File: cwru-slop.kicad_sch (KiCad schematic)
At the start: 44 parts, among them J1 USB_C_Receptacle_USB2.0_16P, J2 FTSH-105-01-L-DV-007-K, SW1 SW_SPDT, U1 TLV9001IDCK, U10 B3U-1000P, U2 AP63205WU, U3 TLV75533PDBV, U4 STM32L433CCTx, U5 TPS2116DRL, U6 FXLS8974CFR3, U7 ESDCAN24-2BLY, U8 MCP2562-E-SN, U9 24lc32at-i/ot, Y1 XRCGB24M000F3M00R0

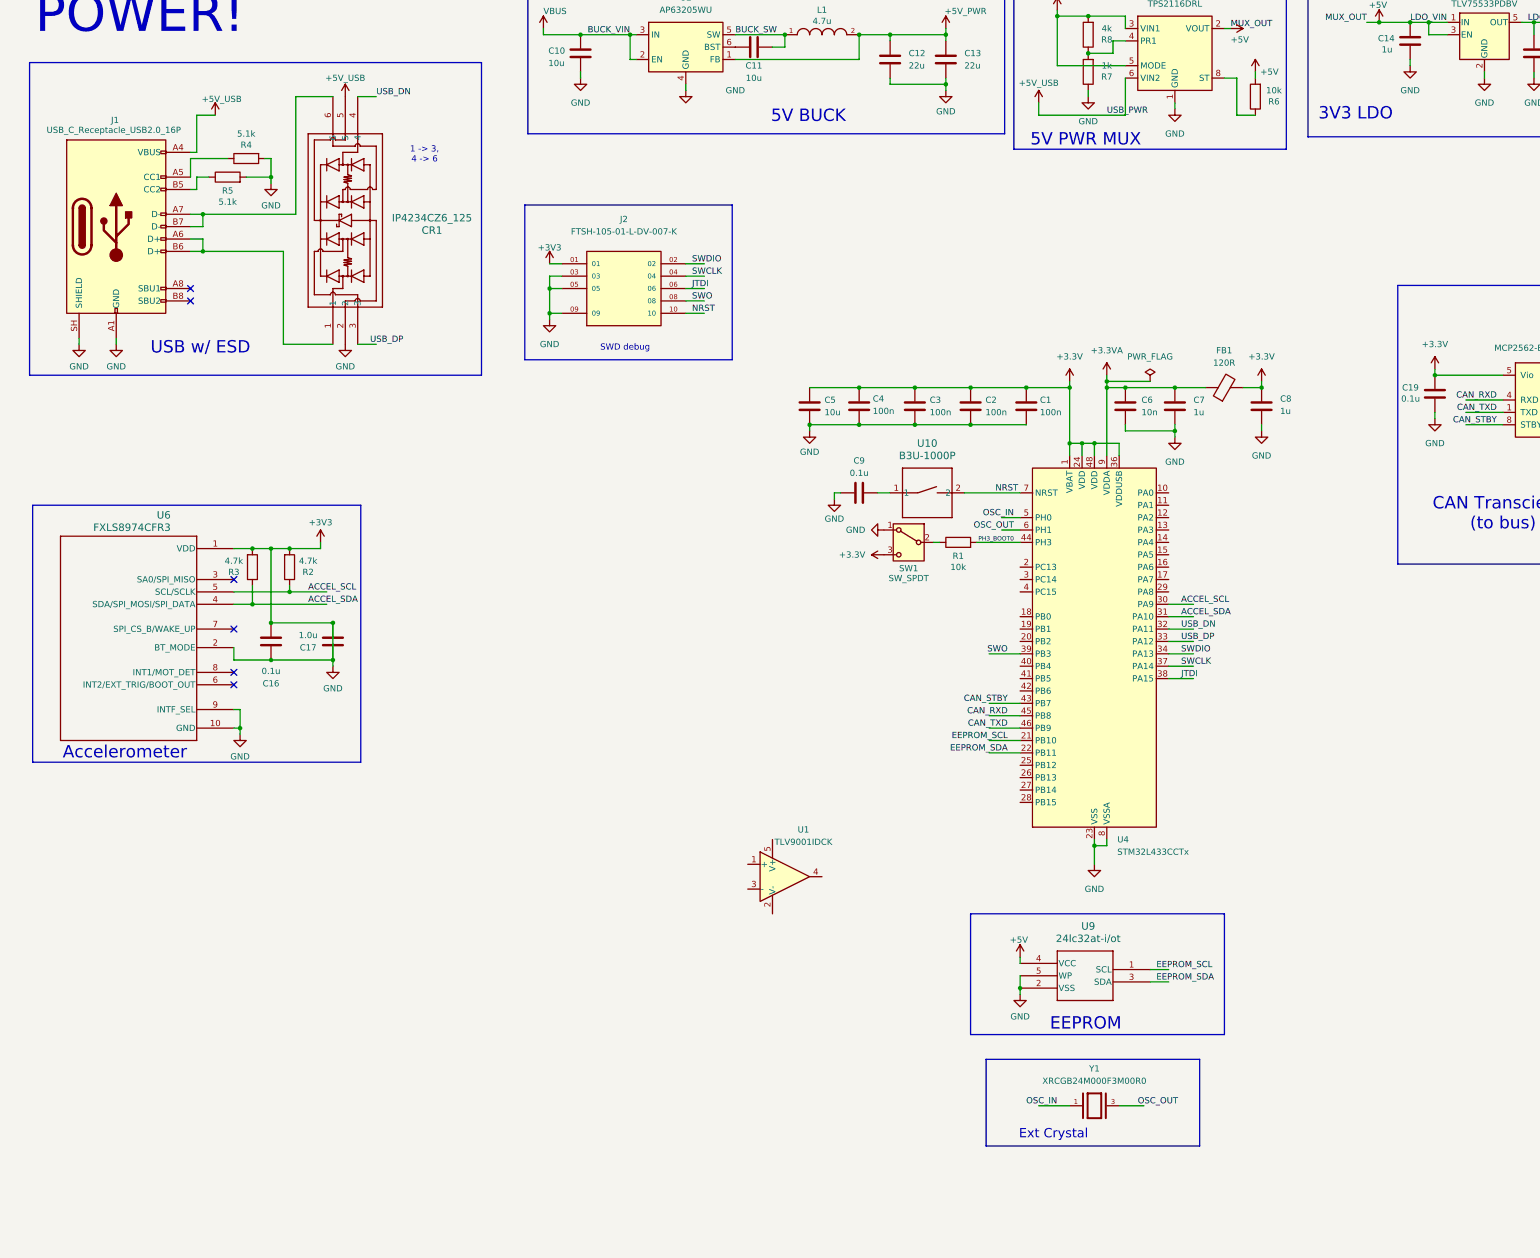
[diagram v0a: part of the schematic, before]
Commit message: analog inputs and filtering
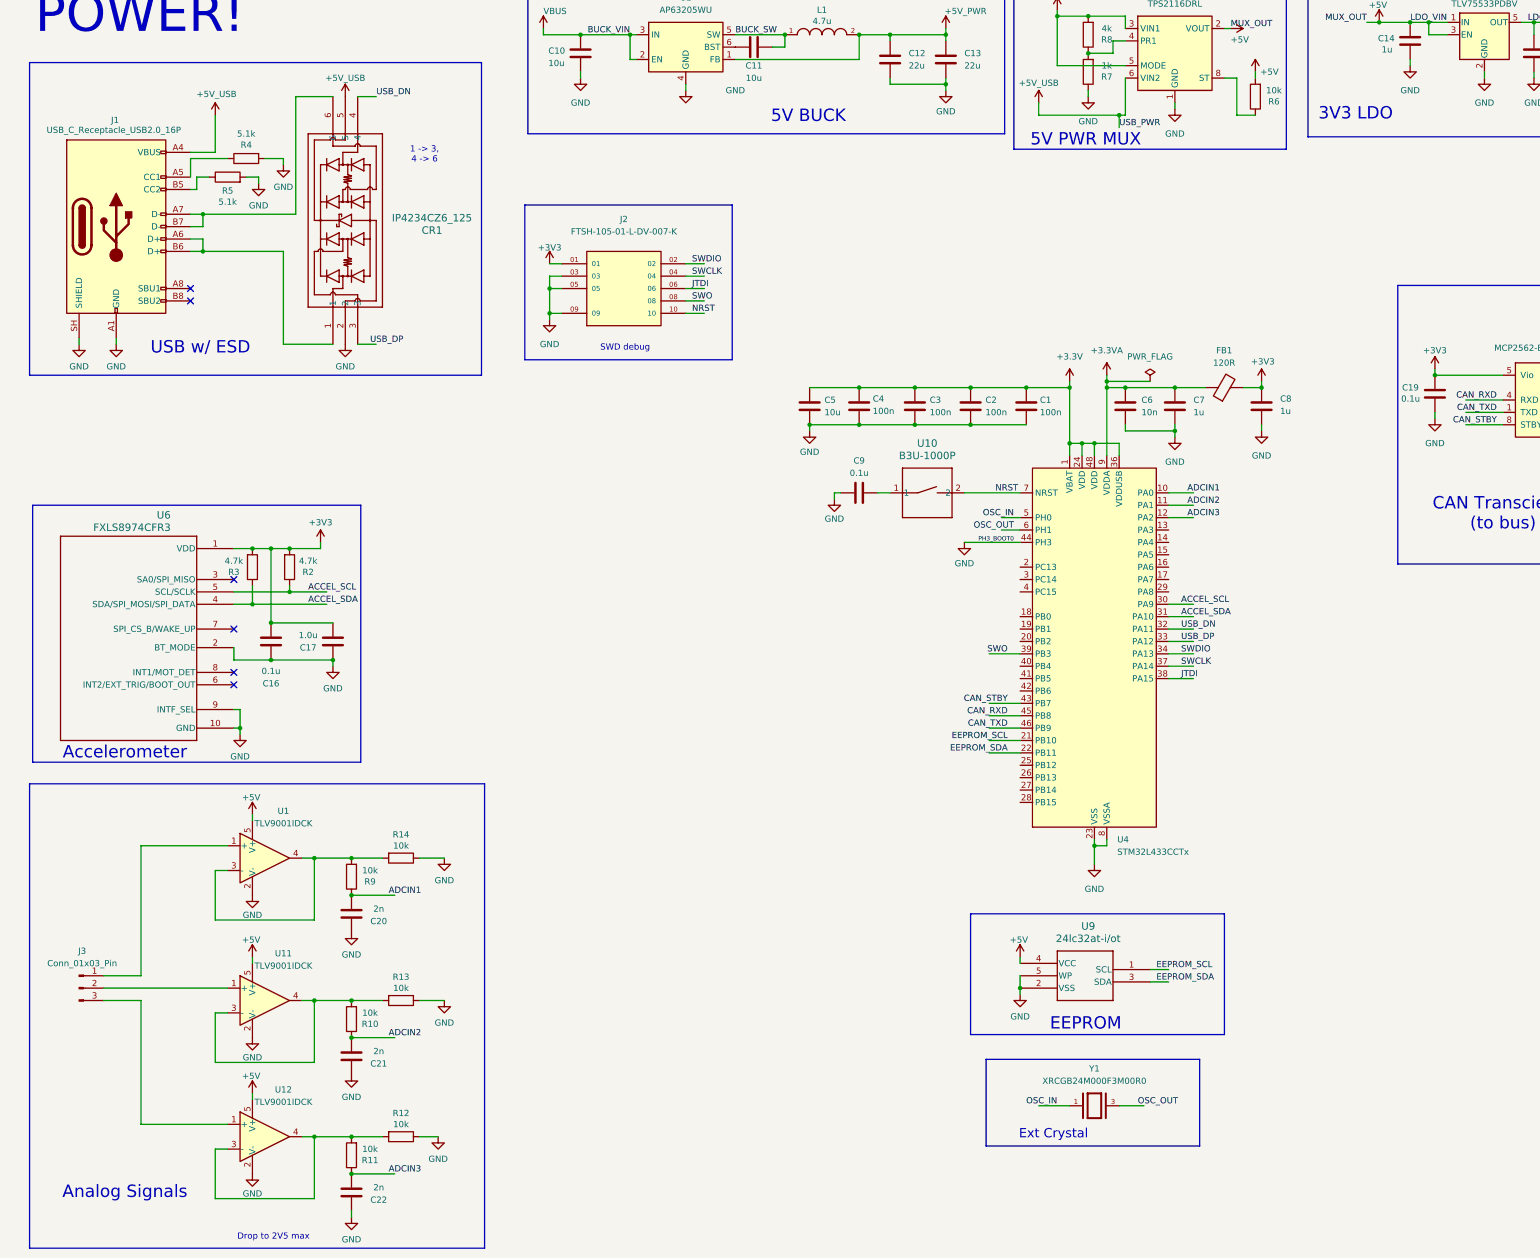
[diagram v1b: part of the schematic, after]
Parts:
- removed R1: 10k, Resistor_SMD:R_0603_1608Metric_Pad0.98x0.95mm_HandSolder, symbol slopp:R
- removed SW1: SW_SPDT, Package_SO:SOIC-28W_7.5x17.9mm_P1.27mm, symbol Switch:SW_SPDT
- added C20, C21, C22: 2n, Capacitor_SMD:C_0603_1608Metric_Pad1.08x0.95mm_HandSolder, symbol slopp:C
- added J3: Conn_01x03_Pin, LED_THT:LED_D5.0mm_IRGrey, symbol Connector:Conn_01x03_Pin
- added R10, R11, R12, R13, R14, R9: 10k, Resistor_SMD:R_0603_1608Metric_Pad0.98x0.95mm_HandSolder, symbol slopp:R
- added U11, U12: TLV9001IDCK, Package_TO_SOT_SMD:SOT-353_SC-70-5, symbol slopp:TLV9001IDCK
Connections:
- net PH3_BOOT0 is gone; now on net GND: U4.44 (PH3)
- net +3.3V: no longer C19.2, C8.1, FB1.2, U8.5 (Vio)
- net +3V3: now also C19.2, C8.1, FB1.2, U8.5 (Vio); no longer C1.2, C10.2, C12.2, C13.1, C14.2, C15.2, C16.1, C17.1, C18.2, C19.1, C2.2, C3.2, C4.2, C5.2, C6.2, C7.2, C8.2, C9.1, CR1.2, J1.A1 (GND), J1.A12 (GND), J1.B1 (GND), J1.B12 (GND), J1.SH (SHIELD), J2.03, J2.05, J2.09, R4.2, R5.2, R7.1, U2.4 (GND), U3.2 (GND), U4.23 (VSS), U4.35 (VSS), U4.47 (VSS), U4.8 (VSSA), U5.1 (GND), U6.10 (GND), U6.2 (BT_MODE), U6.9 (INTF_SEL), U7.3, U8.2 (VSS), U9.2 (VSS), U9.5 (WP)
- net +5V: now also U1.5 (V+), U11.5 (V+), U12.5 (V+)
- net at U1.1 (+): now also J3.1 (Pin_1)
- net GND: now reaches U1.2 (V-)
- net GND: now also C1.2, C10.2, C12.2, C13.1, C14.2, C15.2, C16.1, C17.1, C18.2, C19.1, C2.2, C3.2, C4.2, C5.2, C6.2, C7.2, C8.2, C9.1, CR1.2, J1.A1 (GND), J1.A12 (GND), J1.B1 (GND), J1.B12 (GND), J1.SH (SHIELD), J2.03, J2.05, J2.09, R4.2, R5.2, R7.1, U2.4 (GND), U3.2 (GND), U4.23 (VSS), U4.35 (VSS), U4.47 (VSS), U4.8 (VSSA), U5.1 (GND), U6.10 (GND), U6.2 (BT_MODE), U6.9 (INTF_SEL), U7.3, U8.2 (VSS), U9.2 (VSS), U9.5 (WP), C20.1, C21.1, C22.1, R12.1, R13.1, R14.1, U11.2 (V-), U12.2 (V-)
- net at U1.3 (-): now also U1.4, R14.2, R9.2
- net ADCIN1: now reaches U4.10 (PA0)
- net ADCIN1: now also C20.2, R9.1
- net ADCIN2: now reaches U4.11 (PA1)
- net ADCIN2: now also C21.2, R10.1
- net ADCIN3: now reaches U4.12 (PA2)
- net ADCIN3: now also C22.2, R11.1
- new net: R11.2, R12.2, U12.3 (-), U12.4
- new net: R10.2, R13.2, U11.3 (-), U11.4
- new net: J3.3 (Pin_3), U12.1 (+)
- new net: J3.2 (Pin_2), U11.1 (+)
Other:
- note added: "Analog Signals"
- note added: "Drop to 2V5 max"
- moved on the sheet: U1

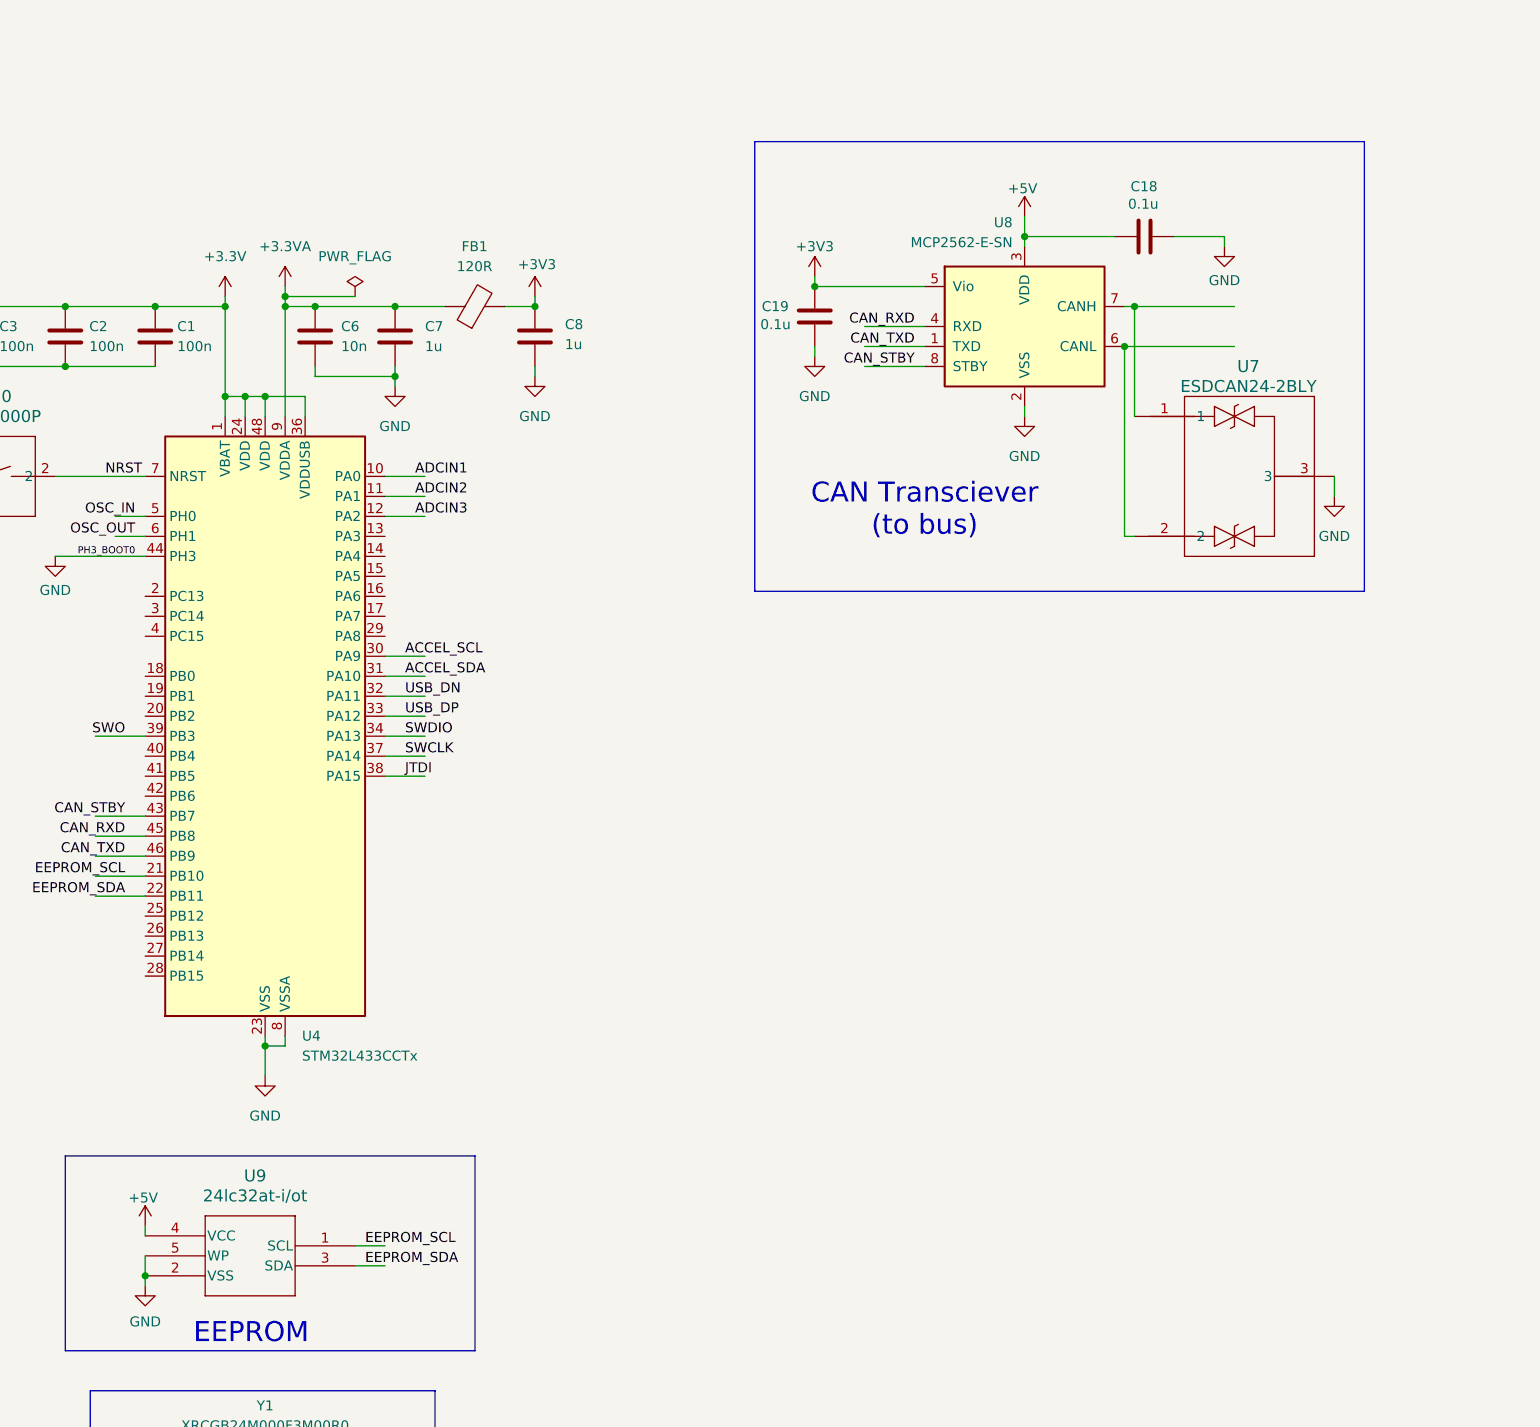
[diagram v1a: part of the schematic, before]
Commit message: add connector for can bus
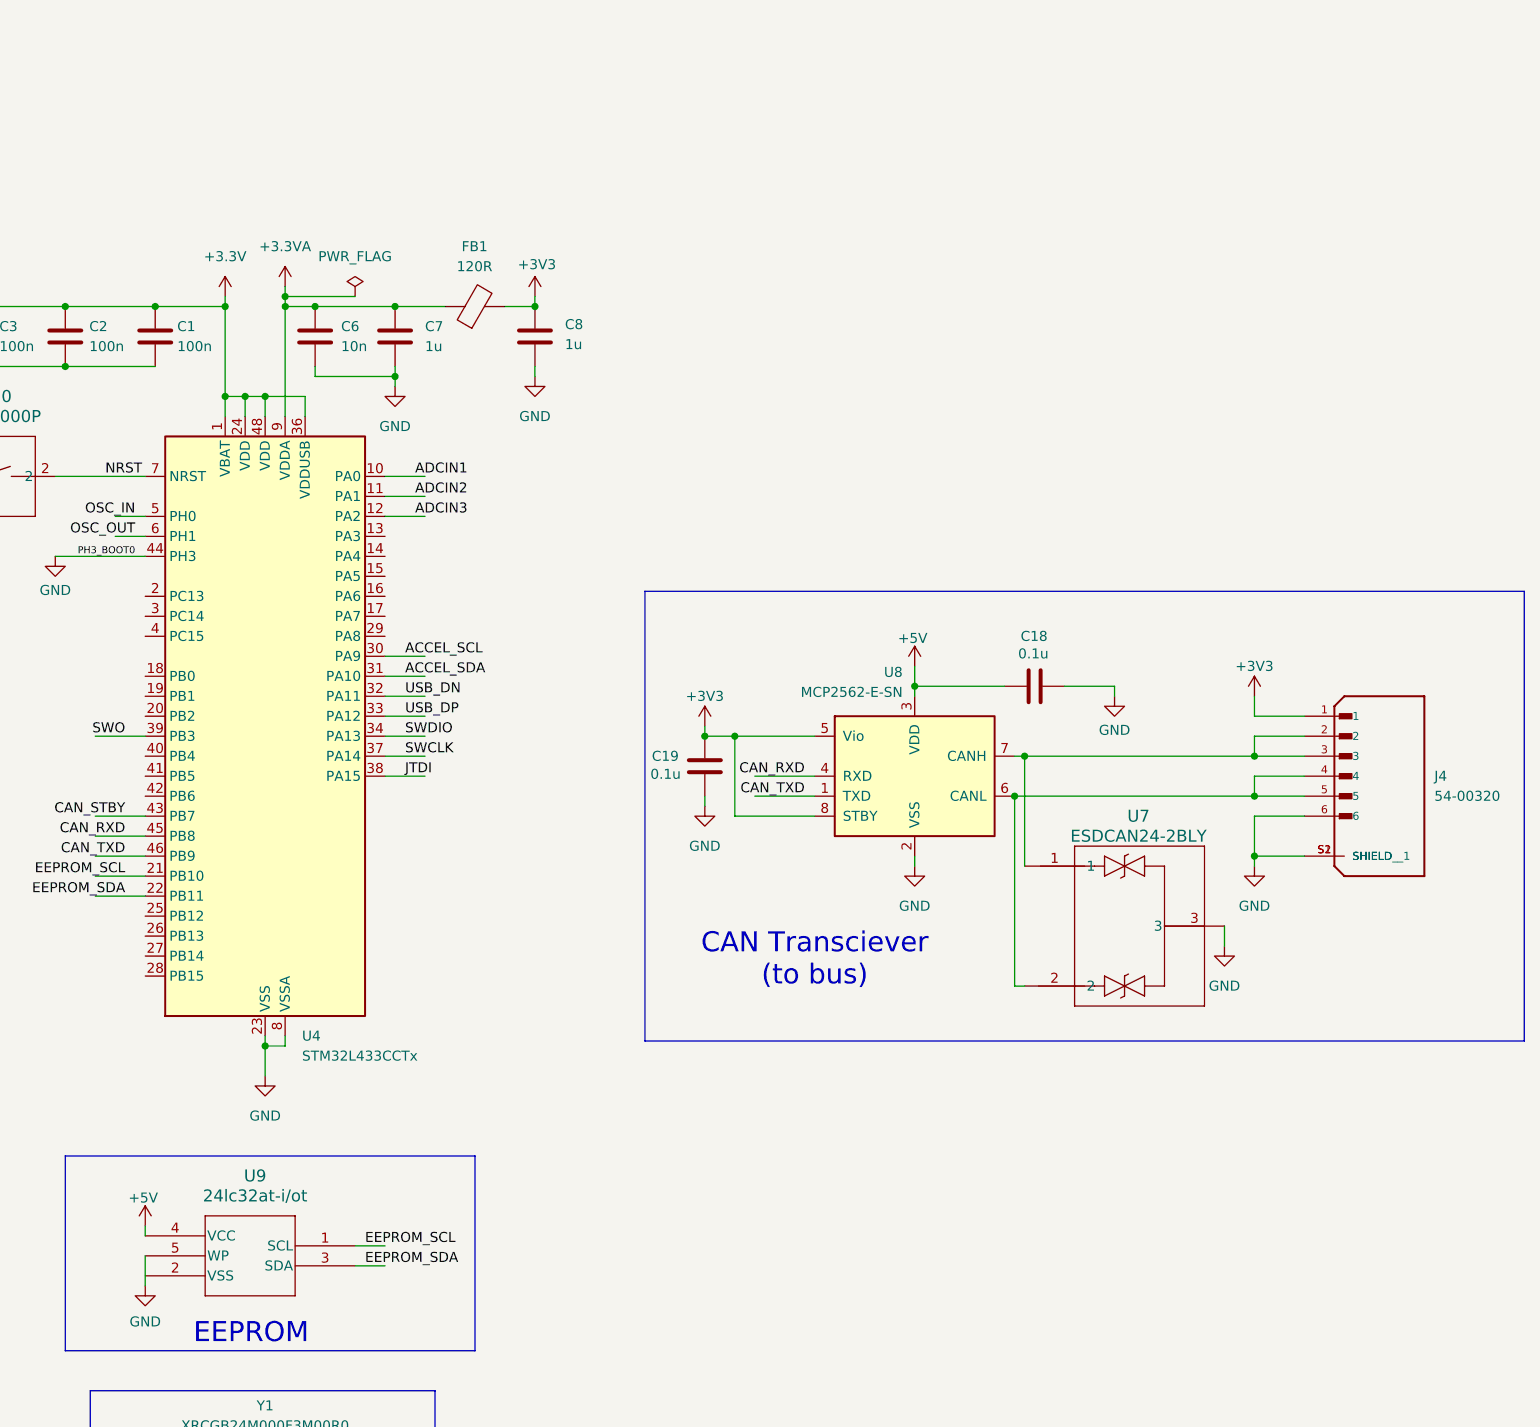
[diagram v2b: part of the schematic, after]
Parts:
- added J4: 54-00320, 54-00320:TENSILITY_54-00320, symbol slopp:54-00320
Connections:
- net +3V3: now also U8.8 (STBY), J4.1
- net CAN_STBY: no longer U8.8 (STBY)
- net GND: now also J4.6, J4.S1 (SHIELD), J4.S2 (SHIELD__1); no longer U9.2 (VSS)
- net at U7.2, U8.6 (CANL): now also J4.4, J4.5
- net at U7.1, U8.7 (CANH): now also J4.2, J4.3
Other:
- moved on the sheet: C18, C19, U7, U8

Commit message: crystal load caps and smalls
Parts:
- added C23, C24: 6p, Capacitor_SMD:C_0603_1608Metric_Pad1.08x0.95mm_HandSolder, symbol slopp:C
- added R15: 10k, Resistor_SMD:R_0603_1608Metric_Pad0.98x0.95mm_HandSolder, symbol slopp:R
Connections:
- net +3V3: no longer U8.8 (STBY)
- net +5V: now also R15.2
- net GND: now also C23.1, C24.1
- net OSC_IN: now also C23.2
- net OSC_OUT: now also C24.2
- net BUCK_SW: no longer names the net of C11.2, L1.1, U2.5 (SW)
- new net: R15.1, U8.8 (STBY)
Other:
- moved on the sheet: C18, C19, J4, U7, U8
